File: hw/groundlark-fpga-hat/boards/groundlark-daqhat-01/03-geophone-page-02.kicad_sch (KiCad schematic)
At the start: 6 parts

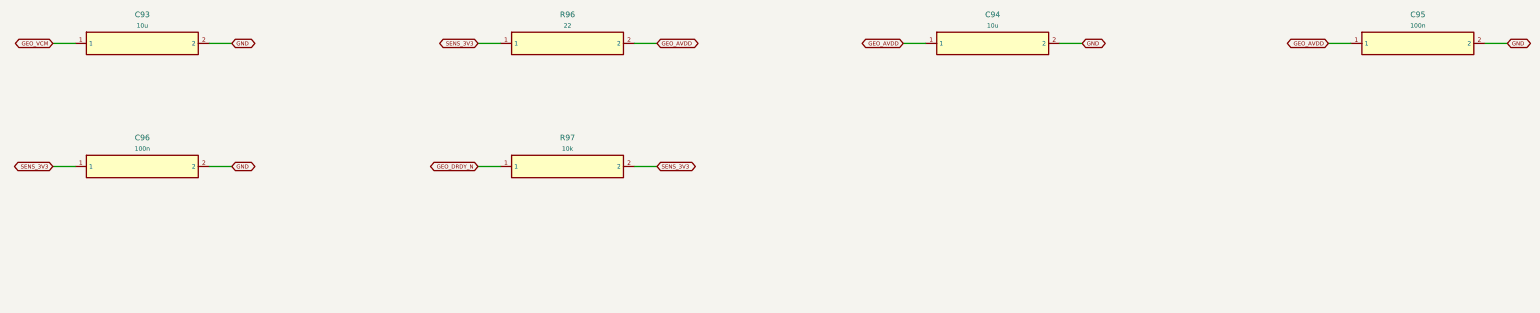
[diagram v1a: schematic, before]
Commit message: Add Groundlark GNSS timing, SMA access and calibration workflow
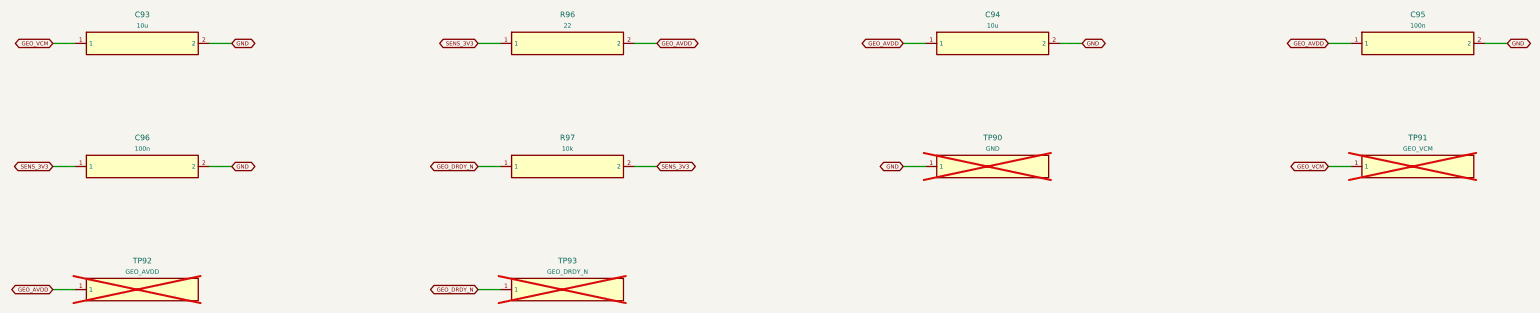
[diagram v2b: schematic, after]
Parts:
- added TP90: GND, Groundlark:TestPoint__TestPoint_Pad_D1.5mm, symbol Groundlark:Part_TP90
- added TP91: GEO_VCM, Groundlark:TestPoint__TestPoint_Pad_D1.5mm, symbol Groundlark:Part_TP91
- added TP92: GEO_AVDD, Groundlark:TestPoint__TestPoint_Pad_D1.5mm, symbol Groundlark:Part_TP92
- added TP93: GEO_DRDY_N, Groundlark:TestPoint__TestPoint_Pad_D1.5mm, symbol Groundlark:Part_TP93
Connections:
- net GEO_AVDD: now also TP92.1
- net GEO_DRDY_N: now also TP93.1
- net GEO_VCM: now also TP91.1
- net GND: now also TP90.1
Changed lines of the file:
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@@
 (wire (pts (xy 162.56 66.04) (xy 167.64 66.04)) (stroke (width 0) (type default)))
 (global_label "SENS_3V3" (shape bidirectional) (at 167.64 66.04 0) (effects (font (size 0.9 0.9)) (justify left)))
+(symbol (lib_id "Groundlark:Part_TP90") (at 243.83999999999997 66.04 0) (unit 1) (in_bom yes) (on_board yes) (dnp yes)
+              (property "Reference" "TP90" (at 243.83999999999997 59.5 0) (effects (font (size 1.27 1.27))))
+              (property "Value" "GND" (at 243.83999999999997 62.0 0) (effects (font (size 1.0 1.0))))
+              (property "Footprint" "Groundlark:TestPoint__TestPoint_Pad_D1.5mm" (at 243.83999999999997 66.04 0) (effects (font (size 1 1)) hide))
+              (property "MPN" "PCB copper" (at 243.83999999999997 66.04 0) (effects (font (size 1 1)) hide))
+              (instances (project "groundlark-daqhat-01" (path "/de5c43d7-546f-5b4d-b587-d8dfceb38170/f0acbc83-58d7-5697-b933-1154f21f83d0" (reference "TP90") (unit 1)))))
+(wire (pts (xy 228.6 66.04) (xy 223.52 66.04)) (stroke (width 0) (type default)))
+(global_label "GND" (shape bidirectional) (at 223.52 66.04 180) (effects (font (size 0.9 0.9)) (justify right)))
+(symbol (lib_id "Groundlark:Part_TP91") (at 340.35999999999996 66.04 0) (unit 1) (in_bom yes) (on_board yes) (dnp yes)
+              (property "Reference" "TP91" (at 340.35999999999996 59.5 0) (effects (font (size 1.27 1.27))))
+              (property "Value" "GEO_VCM" (at 340.35999999999996 62.0 0) (effects (font (size 1.0 1.0))))
+              (property "Footprint" "Groundlark:TestPoint__TestPoint_Pad_D1.5mm" (at 340.35999999999996 66.04 0) (effects (font (size 1 1)) hide))
+              (property "MPN" "PCB copper" (at 340.35999999999996 66.04 0) (effects (font (size 1 1)) hide))
+              (instances (project "groundlark-daqhat-01" (path "/de5c43d7-546f-5b4d-b587-d8dfceb38170/f0acbc83-58d7-5697-b933-1154f21f83d0" (reference "TP91") (unit 1)))))
+(wire (pts (xy 325.12 66.04) (xy 320.04 66.04)) (stroke (width 0) (type default)))
+(global_label "GEO_VCM" (shape bidirectional) (at 320.04 66.04 180) (effects (font (size 0.9 0.9)) (justify right)))
+(symbol (lib_id "Groundlark:Part_TP92") (at 50.8 93.98 0) (unit 1) (in_bom yes) (on_board yes) (dnp yes)
+              (property "Reference" "TP92" (at 50.8 87.44 0) (effects (font (size 1.27 1.27))))
+              (property "Value" "GEO_AVDD" (at 50.8 89.94 0) (effects (font (size 1.0 1.0))))
+              (property "Footprint" "Groundlark:TestPoint__TestPoint_Pad_D1.5mm" (at 50.8 93.98 0) (effects (font (size 1 1)) hide))
+              (property "MPN" "PCB copper" (at 50.8 93.98 0) (effects (font (size 1 1)) hide))
+              (instances (project "groundlark-daqhat-01" (path "/de5c43d7-546f-5b4d-b587-d8dfceb38170/f0acbc83-58d7-5697-b933-1154f21f83d0" (reference "TP92") (unit 1)))))
+(wire (pts (xy 35.56 93.98) (xy 30.48 93.98)) (stroke (width 0) (type default)))
+(global_label "GEO_AVDD" (shape bidirectional) (at 30.48 93.98 180) (effects (font (size 0.9 0.9)) (justify right)))
+(symbol (lib_id "Groundlark:Part_TP93") (at 147.32 93.98 0) (unit 1) (in_bom yes) (on_board yes) (dnp yes)
+              (property "Reference" "TP93" (at 147.32 87.44 0) (effects (font (size 1.27 1.27))))
+              (property "Value" "GEO_DRDY_N" (at 147.32 89.94 0) (effects (font (size 1.0 1.0))))
+              (property "Footprint" "Groundlark:TestPoint__TestPoint_Pad_D1.5mm" (at 147.32 93.98 0) (effects (font (size 1 1)) hide))
+              (property "MPN" "PCB copper" (at 147.32 93.98 0) (effects (font (size 1 1)) hide))
+              (instances (project "groundlark-daqhat-01" (path "/de5c43d7-546f-5b4d-b587-d8dfceb38170/f0acbc83-58d7-5697-b933-1154f21f83d0" (reference "TP93") (unit 1)))))
+(wire (pts (xy 132.08 93.98) (xy 127.0 93.98)) (stroke (width 0) (type default)))
+(global_label "GEO_DRDY_N" (shape bidirectional) (at 127.0 93.98 180) (effects (font (size 0.9 0.9)) (justify right)))
 )
